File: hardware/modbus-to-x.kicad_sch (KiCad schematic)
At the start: 50 parts, among them J1 PWR, J2 UART, SW1 SW_Push, SW2 SW_Push, U1 AMS1117-3.3, U3 MAX3485, U4 ESP32-WROOM-32D, U5 AT24CS64-XHM, U6 AT24CS64-XHM, U7 LMR14020SQDPRTQ1

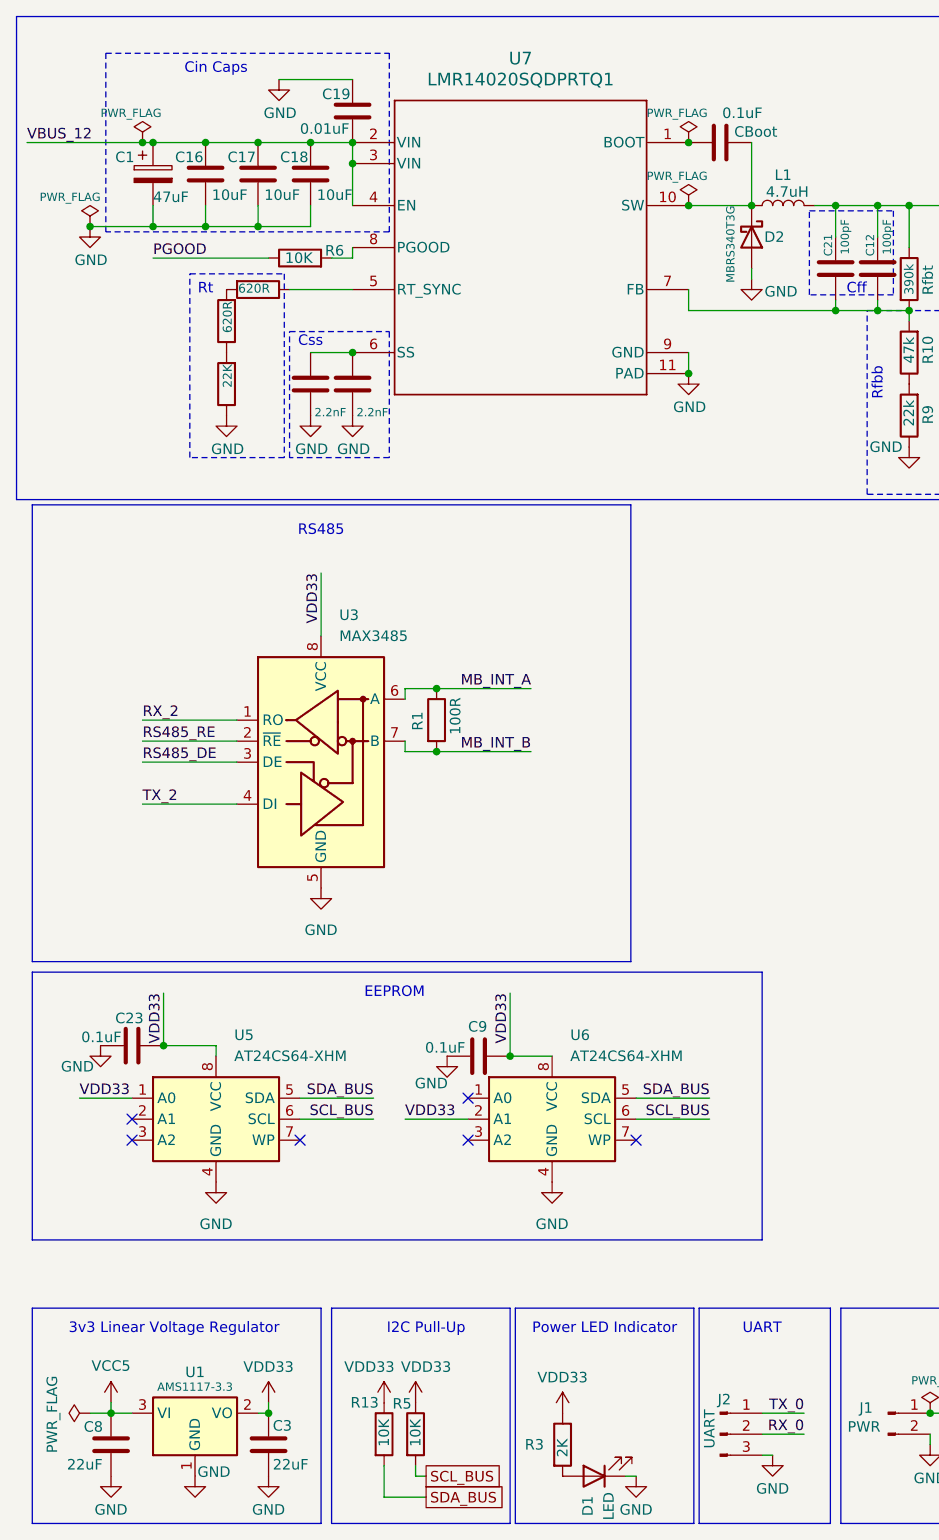
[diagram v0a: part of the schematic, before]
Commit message: updated footprints
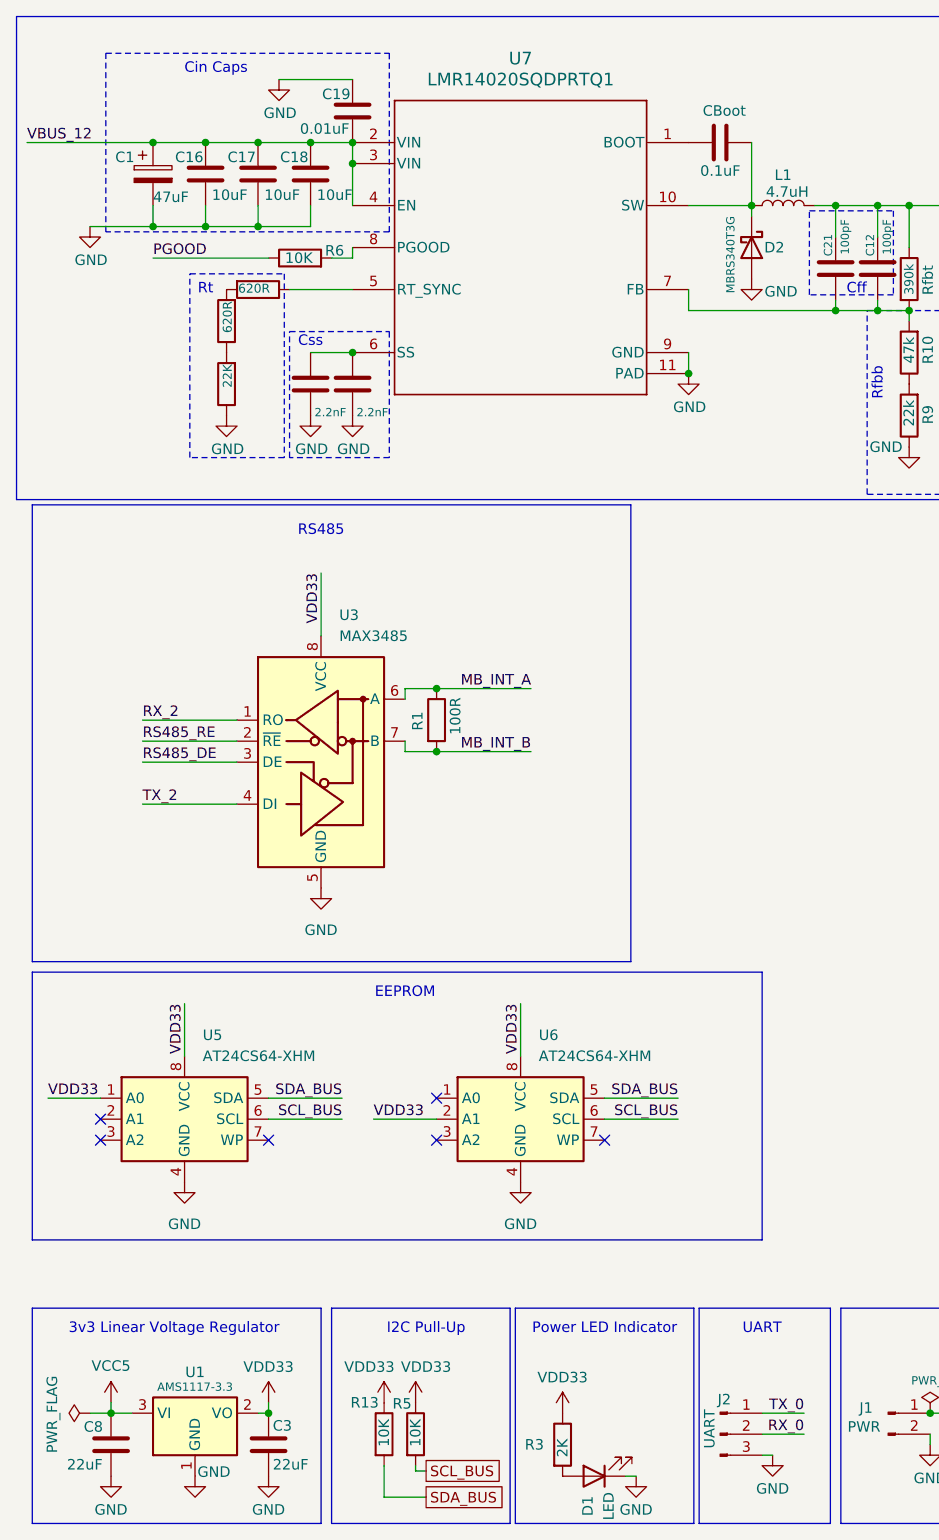
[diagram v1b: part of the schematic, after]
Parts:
- removed C23, C9: 0.1uF, Capacitor_SMD:C_1206_3216Metric_Pad1.33x1.80mm_HandSolder, symbol Device:C
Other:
- moved on the sheet: D2, U5, U6
